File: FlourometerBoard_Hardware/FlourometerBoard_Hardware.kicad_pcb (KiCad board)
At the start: 2 copper layers, 105.4 x 36.8 mm, 14 parts, among them J1 RJ45_LED_Shielded, U1 Teensy4.1_DEV-16771, U3 OKI

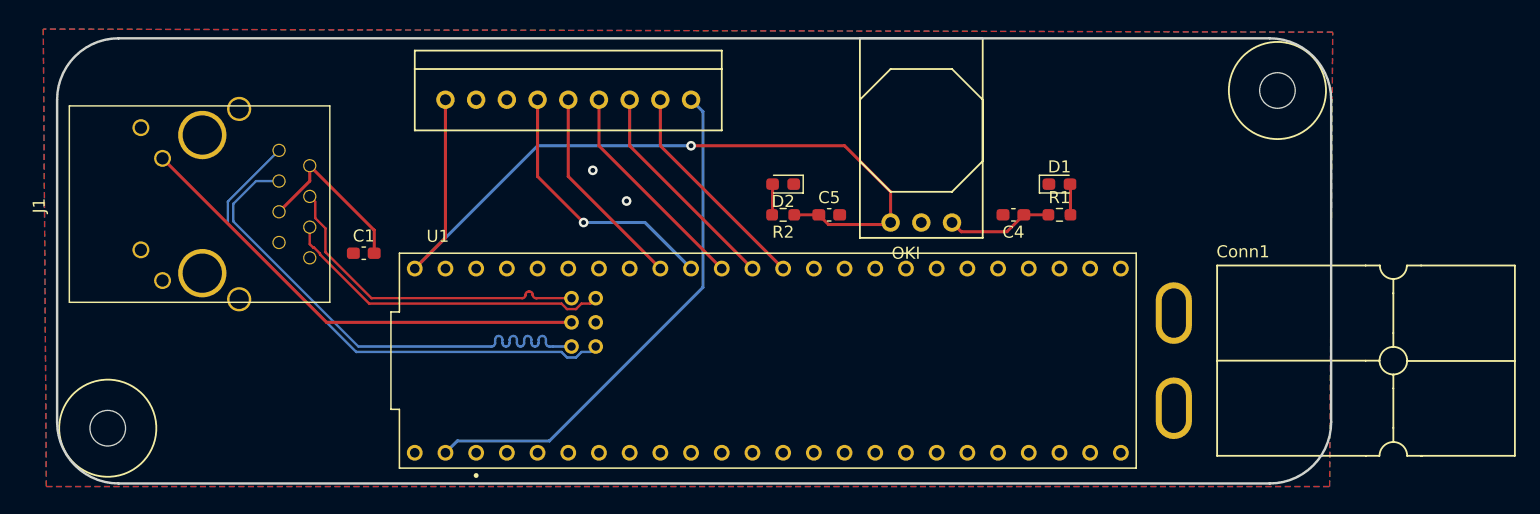
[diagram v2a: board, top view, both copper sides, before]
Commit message: Added LED Breakout Connector to Fluoro Board
Also updated footprint for both boards
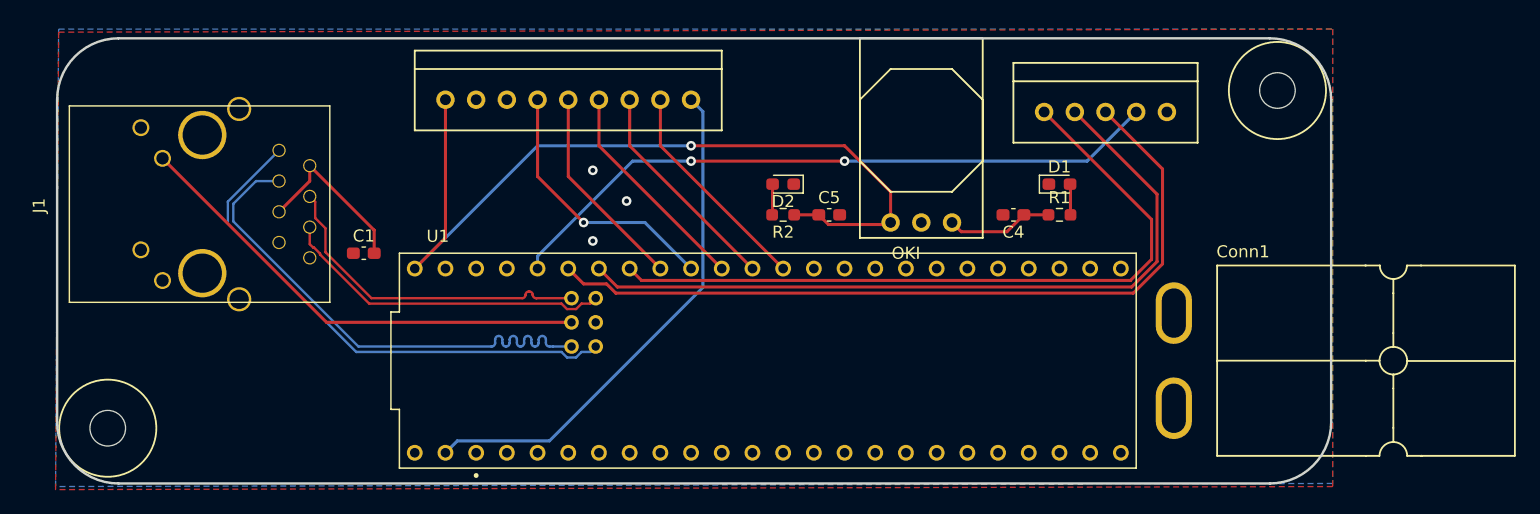
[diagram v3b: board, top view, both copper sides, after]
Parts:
- added Conn3: Molex_SL_05, MRDT_Connectors:MOLEX_SL_05_Vertical, F.Cu at (120.7, 87.4)
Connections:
- net +3V3 renamed +5V
- U1 pad 19: unconnected-(U1-A5-Pad19) -> 530nm LED
- U1 pad 20: unconnected-(U1-A6-Pad20) -> 522nm LED
- U1 pad 21: unconnected-(U1-A7-Pad21) -> 430nm LED
- U1 pad 22: unconnected-(U1-A8-Pad22) -> 400nm LED
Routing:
- net 430nm LED: track 0.00 -> 65.5 mm
- net 522nm LED: track 0.00 -> 62.9 mm
- net 530nm LED: track 0.00 -> 60.2 mm
- net 400nm LED: track 0.00 -> 55.5 mm, vias 0 -> 2
- net GND: vias 2 -> 3
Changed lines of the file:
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@@
   (net 2 "Net-(C1-Pad2)")
   (net 3 "+12V")
-  (net 4 "+3V3")
+  (net 4 "+5V")
   (net 5 "EOS")
   (net 6 "TRG")
@@
   (net 33 "unconnected-(U1-MISO-Pad12)")
   (net 34 "unconnected-(U1-SCK-Pad13)")
-  (net 35 "unconnected-(U1-A5-Pad19)")
-  (net 36 "unconnected-(U1-A6-Pad20)")
-  (net 37 "unconnected-(U1-A7-Pad21)")
-  (net 38 "unconnected-(U1-A8-Pad22)")
+  (net 35 "530nm LED")
+  (net 36 "522nm LED")
+  (net 37 "430nm LED")
+  (net 38 "400nm LED")
   (net 39 "unconnected-(U1-A9-Pad23)")
   (net 40 "unconnected-(U1-A10-Pad24)")
@@
       (stroke (width 0.15) (type solid)) (layer "F.SilkS"))
     (pad "1" thru_hole circle (at 0 0) (size 1.524 1.524) (drill 0.9) (layers "*.Cu" "*.Mask")
-      (net 4 "+3V3") (pintype "input"))
+      (net 4 "+5V") (pintype "input"))
     (pad "2" thru_hole circle (at 2.54 0) (size 1.524 1.524) (drill 0.9) (layers "*.Cu" "*.Mask")
       (net 1 "GND") (pintype "input"))
@@
       (net 1 "GND") (pinfunction "GND") (pintype "output"))
     (pad "3" thru_hole circle (at 5.08 0 180) (size 1.524 1.524) (drill 0.889) (layers "*.Cu" "*.Mask")
-      (net 4 "+3V3") (pinfunction "Vo") (pintype "output"))
+      (net 4 "+5V") (pinfunction "Vo") (pintype "output"))
     (model "${MRDT_KICAD_LIBRARIES}/3D Files/MRDT_Devices/OKI.stp"
       (offset (xyz -2.793999958 1.269999981 3.809999943))
@@
       (net 6 "TRG") (pinfunction "A4") (pintype "bidirectional"))
     (pad "19" thru_hole circle (at -11.43 -7.62) (size 1.308 1.308) (drill 0.8) (layers "*.Cu" "*.Mask")
-      (net 35 "unconnected-(U1-A5-Pad19)") (pinfunction "A5") (pintype "bidirectional+no_connect"))
+      (net 35 "530nm LED") (pinfunction "A5") (pintype "bidirectional"))
     (pad "20" thru_hole circle (at -13.97 -7.62) (size 1.308 1.308) (drill 0.8) (layers "*.Cu" "*.Mask")
-      (net 36 "unconnected-(U1-A6-Pad20)") (pinfunction "A6") (pintype "bidirectional+no_connect"))
+      (net 36 "522nm LED") (pinfunction "A6") (pintype "bidirectional"))
     (pad "21" thru_hole circle (at -16.51 -7.62) (size 1.308 1.308) (drill 0.8) (layers "*.Cu" "*.Mask")
-      (net 37 "unconnected-(U1-A7-Pad21)") (pinfunction "A7") (pintype "bidirectional+no_connect"))
+      (net 37 "430nm LED") (pinfunction "A7") (pintype "bidirectional"))
     (pad "22" thru_hole circle (at -19.05 -7.62) (size 1.308 1.308) (drill 0.8) (layers "*.Cu" "*.Mask")
-      (net 38 "unconnected-(U1-A8-Pad22)") (pinfunction "A8") (pintype "bidirectional+no_connect"))
+      (net 38 "400nm LED") (pinfunction "A8") (pintype "bidirectional"))
     (pad "23" thru_hole circle (at -21.59 -7.62) (size 1.308 1.308) (drill 0.8) (layers "*.Cu" "*.Mask")
       (net 39 "unconnected-(U1-A9-Pad23)") (pinfunction "A9") (pintype "bidirectional+no_connect"))
@@
       (net 17 "T-") (pinfunction "T-") (pintype "bidirectional"))
     (pad "VIN" thru_hole circle (at -29.21 -7.62) (size 1.308 1.308) (drill 0.8) (layers "*.Cu" "*.Mask")
-      (net 4 "+3V3") (pinfunction "VIN") (pintype "input"))
+      (net 4 "+5V") (pinfunction "VIN") (pintype "input"))
     (model "${MRDT_KICAD_LIBRARIES}/3D Files/MRDT_Shields/DEV-16771--3DModel-STEP-418109.STEP"
       (offset (xyz 0 0 0))
@@
       (stroke (width 0.1) (type solid)) (layer "F.Fab"))
     (pad "1" smd roundrect (at -0.8625 0) (size 1.075 0.95) (layers "F.Cu" "F.Paste" "F.Mask") (roundrect_rratio 0.25)
-      (net 4 "+3V3") (pintype "passive"))
+      (net 4 "+5V") (pintype "passive"))
     (pad "2" smd roundrect (at 0.8625 0) (size 1.075 0.95) (layers "F.Cu" "F.Paste" "F.Mask") (roundrect_rratio 0.25)
       (net 1 "GND") (pintype "passive"))
@@
       (stroke (width 0.1) (type solid)) (layer "F.Fab"))
     (pad "1" smd roundrect (at -0.9125 0 180) (size 0.975 0.95) (layers "F.Cu" "F.Paste" "F.Mask") (roundrect_rratio 0.25)
-      (net 4 "+3V3") (pintype "passive"))
+      (net 4 "+5V") (pintype "passive"))
     (pad "2" smd roundrect (at 0.9125 0 180) (size 0.975 0.95) (layers "F.Cu" "F.Paste" "F.Mask") (roundrect_rratio 0.25)
       (net 12 "Net-(D2-A)") (pintype "passive"))
@@
       (scale (xyz 1 1 1))
       (rotate (xyz 0 0 0))
+    )
+  )
+  (footprint "MRDT_Connectors:MOLEX_SL_05_Vertical" (layer "F.Cu")
+    (at 120.65 87.376)
+    (property "Sheetfile" "FlourometerBoard_Hardware.kicad_sch")
+    (property "Sheetname" "")
+    (property "ki_keywords" "MOLEX SL")
+    (attr through_hole)
+    (fp_text reference "Conn3" (at -0.635 3.302) (layer "F.SilkS") hide
+        (effects (font (size 1 1) (thickness 0.15)))
+    )
+    (fp_text value "Molex_SL_05" (at 5.08 3.302) (layer "F.Fab")
+        (effects (font (size 1 1) (thickness 0.15)))
+    )
+    (fp_line (start -2.54 -4.064) (end -2.54 -2.54)
+      (stroke (width 0.15) (type solid)) (layer "F.SilkS"))
+    (fp_line (start -2.54 -2.54) (end 12.7 -2.54)
+      (stroke (width 0.15) (type solid)) (layer "F.SilkS"))
+    (fp_line (start -2.54 2.54) (end -2.54 -2.54)
+      (stroke (width 0.15) (type solid)) (layer "F.SilkS"))
+    (fp_line (start 12.7 -4.064) (end -2.54 -4.064)
+      (stroke (width 0.15) (type solid)) (layer "F.SilkS"))
+    (fp_line (start 12.7 -2.54) (end 12.7 -4.064)
+      (stroke (width 0.15) (type solid)) (layer "F.SilkS"))
+    (fp_line (start 12.7 2.54) (end -2.54 2.54)
+      (stroke (width 0.15) (type solid)) (layer "F.SilkS"))
+    (fp_line (start 12.7 2.54) (end 12.7 -2.54)
+      (stroke (width 0.15) (type solid)) (layer "F.SilkS"))
+    (pad "1" thru_hole circle (at 0 0) (size 1.524 1.524) (drill 0.9) (layers "*.Cu" "*.Mask")
+      (net 35 "530nm LED") (pintype "input"))
+    (pad "2" thru_hole circle (at 2.54 0) (size 1.524 1.524) (drill 0.9) (layers "*.Cu" "*.Mask")
+      (net 36 "522nm LED") (pintype "input"))
+    (pad "3" thru_hole circle (at 5.08 0) (size 1.524 1.524) (drill 0.9) (layers "*.Cu" "*.Mask")
+      (net 37 "430nm LED") (pintype "input"))
+    (pad "4" thru_hole circle (at 7.62 0) (size 1.524 1.524) (drill 0.9) (layers "*.Cu" "*.Mask")
+      (net 38 "400nm LED") (pintype "input"))
+    (pad "5" thru_hole circle (at 10.16 0) (size 1.524 1.524) (drill 0.9) (layers "*.Cu" "*.Mask")
+      (net 1 "GND") (pintype "input"))
+    (model "${MRDT_KICAD_LIBRARIES}/3D Files/MRDT_Connctors/Molex_SL_05_Vertical.stp"
+      (offset (xyz -2.539999962 -2.539999962 13.3349998))
+      (scale (xyz 1 1 1))
+      (rotate (xyz 90 0 0))
     )
   )
@@
   (gr_arc (start 144.399 113.03) (mid 142.911102 116.622102) (end 139.319 118.11)
     (stroke (width 0.2) (type default)) (layer "Edge.Cuts"))
+  (via (at 83.312 98.044) (size 0.8) (drill 0.4) (layers "F.Cu" "B.Cu") (free) (net 1))
   (via (at 83.312 92.202) (size 0.8) (drill 0.4) (layers "F.Cu" "B.Cu") (free) (net 1))
   (via (at 86.106 94.742) (size 0.8) (drill 0.4) (layers "F.Cu" "B.Cu") (free) (net 1))
@@
   (segment (start 82.37845 103.23) (end 83.1 103.23) (width 0.2) (layer "F.Cu") (net 20))
   (segment (start 60.1728 98.591) (end 60.244582 98.591) (width 0.2) (layer "F.Cu") (net 20))
+  (segment (start 129.54 96.266) (end 120.65 87.376) (width 0.254) (layer "F.Cu") (net 35))
+  (segment (start 87.341 101.311) (end 127.797 101.311) (width 0.254) (layer "F.Cu") (net 35))
+  (segment (start 86.36 100.33) (end 87.341 101.311) (width 0.254) (layer "F.Cu") (net 35))
+  (segment (start 127.797 101.311) (end 129.54 99.568) (width 0.254) (layer "F.Cu") (net 35))
+  (segment (start 129.54 99.568) (end 129.54 96.266) (width 0.254) (layer "F.Cu") (net 35))
+  (segment (start 129.994 94.18) (end 123.19 87.376) (width 0.254) (layer "F.Cu") (net 36))
+  (segment (start 85.344 101.854) (end 127.896052 101.854) (width 0.254) (layer "F.Cu") (net 36))
+  (segment (start 127.896052 101.854) (end 129.994 99.756052) (width 0.254) (layer "F.Cu") (net 36))
+  (segment (start 83.82 100.33) (end 85.344 101.854) (width 0.254) (layer "F.Cu") (net 36))
+  (segment (start 129.994 99.756052) (end 129.994 94.18) (width 0.254) (layer "F.Cu") (net 36))
+  (segment (start 130.448 92.094) (end 125.73 87.376) (width 0.254) (layer "F.Cu") (net 37))
+  (segment (start 84.447948 101.6) (end 85.209948 102.362) (width 0.254) (layer "F.Cu") (net 37))
+  (segment (start 81.28 100.33) (end 82.55 101.6) (width 0.254) (layer "F.Cu") (net 37))
+  (segment (start 130.448 99.944104) (end 130.448 92.094) (width 0.254) (layer "F.Cu") (net 37))
+  (segment (start 82.55 101.6) (end 84.447948 101.6) (width 0.254) (layer "F.Cu") (net 37))
+  (segment (start 85.209948 102.362) (end 128.030104 102.362) (width 0.254) (layer "F.Cu") (net 37))
+  (segment (start 128.030104 102.362) (end 130.448 99.944104) (width 0.254) (layer "F.Cu") (net 37))
+  (segment (start 91.44 91.44) (end 104.14 91.44) (width 0.254) (layer "F.Cu") (net 38))
+  (via (at 104.14 91.44) (size 0.8) (drill 0.4) (layers "F.Cu" "B.Cu") (net 38))
+  (via (at 91.44 91.44) (size 0.8) (drill 0.4) (layers "F.Cu" "B.Cu") (net 38))
+  (segment (start 78.74 99.301866) (end 86.601866 91.44) (width 0.254) (layer "B.Cu") (net 38))
+  (segment (start 78.74 100.33) (end 78.74 99.301866) (width 0.254) (layer "B.Cu") (net 38))
+  (segment (start 124.206 91.44) (end 128.27 87.376) (width 0.254) (layer "B.Cu") (net 38))
+  (segment (start 104.14 91.44) (end 124.206 91.44) (width 0.254) (layer "B.Cu") (net 38))
+  (segment (start 86.601866 91.44) (end 91.44 91.44) (width 0.254) (layer "B.Cu") (net 38))
   (zone (net 1) (net_name "GND") (layer "F.Cu") (hatch edge 0.5)
     (connect_pads (clearance 0.5))
@@
     (polygon
       (pts
-        (xy 37.846 80.518)
-        (xy 38.1 118.364)
-        (xy 144.272 118.364)
-        (xy 144.526 80.772)
+        (xy 144.526 80.518)
+        (xy 144.526 118.364)
+        (xy 38.862 118.618)
+        (xy 39.116 80.772)
       )
     )
@@
     (polygon
       (pts
-        (xy 144.272 118.364)
-        (xy 144.526 80.772)
-        (xy 37.846 80.518)
-        (xy 38.1 118.364)
+        (xy 144.526 80.518)
+        (xy 144.526 118.11)
+        (xy 38.862 118.364)
+        (xy 39.116 80.518)
       )
     )

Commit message: Added 5V to LED connectors
Also added FETs to LEDs on breakout.
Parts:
- Conn3: value Molex_SL_05 -> Molex_SL_07; footprint MRDT_Connectors:MOLEX_SL_05_Vertical -> MRDT_Connectors:MOLEX_SL_07_Vertical
- moved Conn3 2.74 mm to (118.1, 88.4)
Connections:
- Conn3 pad 5: GND -> +5V
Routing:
- net +5V: track 71.1 -> 96.5 mm
- net 400nm LED: track 55.5 -> 52.5 mm
- net 530nm LED: track 60.2 -> 62.3 mm
- net 430nm LED: track 65.5 -> 67.7 mm
- net 522nm LED: track 62.9 -> 65.0 mm

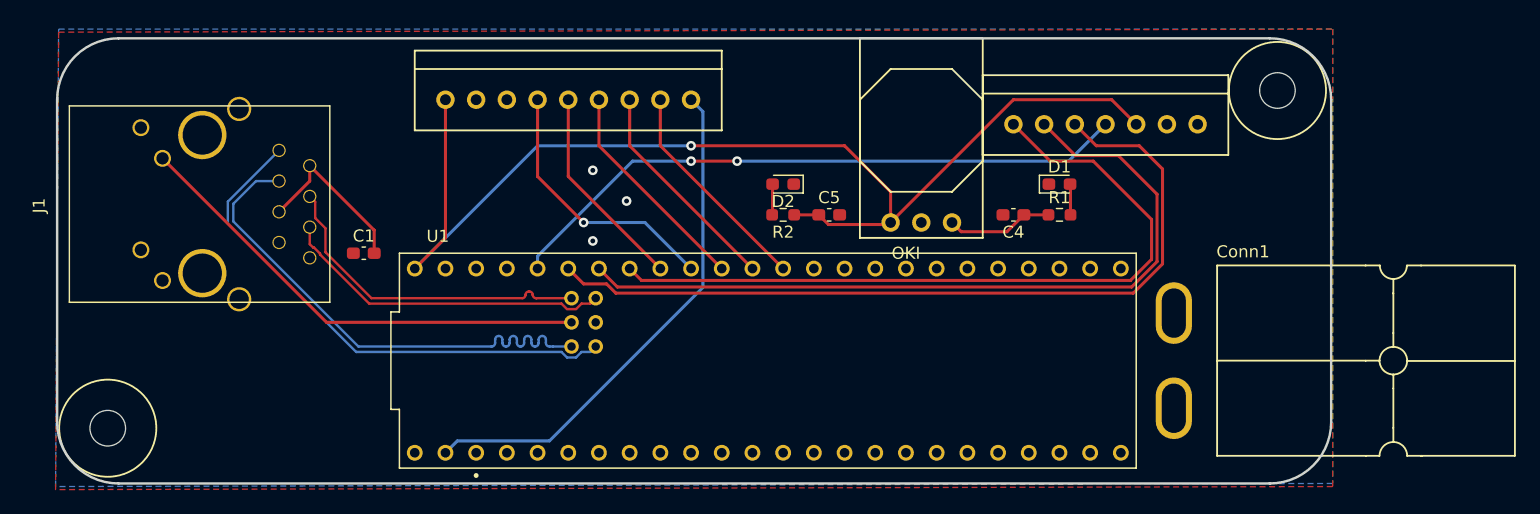
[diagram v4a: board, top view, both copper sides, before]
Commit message: Changes made based on layout review notes
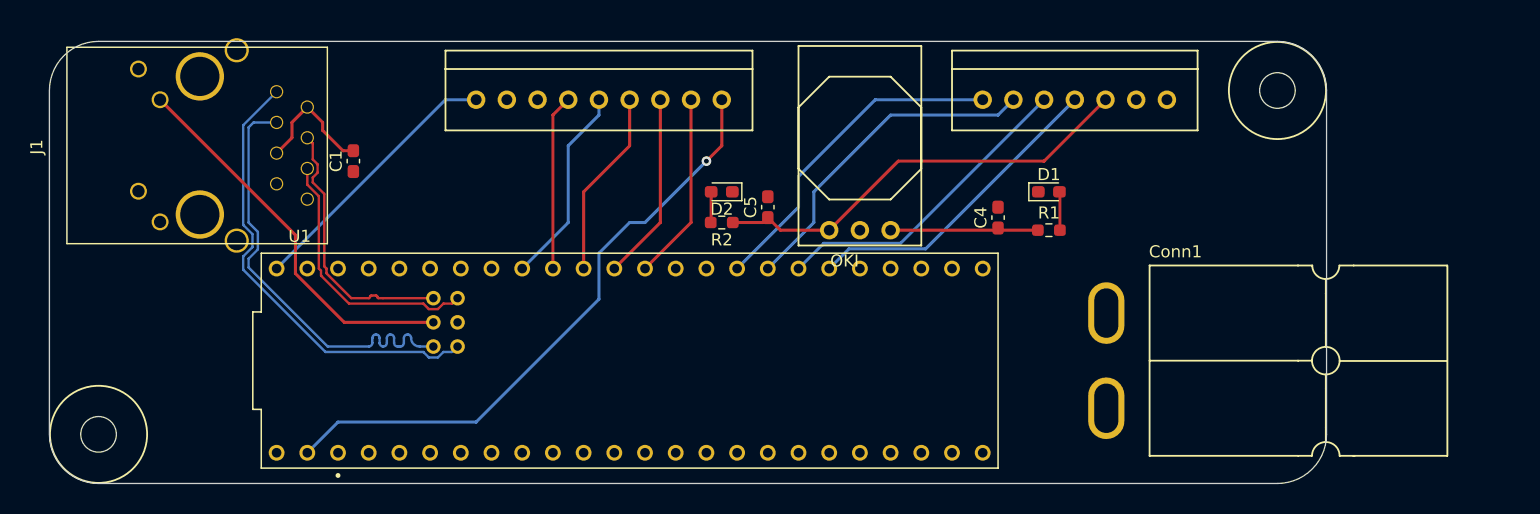
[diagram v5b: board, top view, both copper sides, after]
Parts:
- moved U1 11.4 mm to (86.4, 108.0)
- moved C1 7.67 mm to (63.5, 91.4), turned to 90 degrees
- moved Conn1 5.59 mm to (125.7, 112.2)
- moved C5 5.12 mm to (97.8, 95.2), turned to 90 degrees
- moved D2 5.12 mm to (94.0, 94.0)
- moved U3 5.12 mm to (108.0, 97.2)
- moved R2 5.12 mm to (94.0, 96.5)
- moved J1 4.86 mm to (37.8, 90.3)
- moved Conn3 3.25 mm to (115.6, 86.4)
- moved Conn2 2.54 mm to (73.7, 86.4)
- moved R1 1.54 mm to (121.0, 97.2)
- moved C4 1.29 mm to (116.8, 96.1), turned to 90 degrees
- moved D1 1.08 mm to (121.0, 94.0)
- moved REF** 0.92 mm to (42.4, 114.0)
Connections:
- U1 pad 19: 530nm LED -> unconnected-(U1-A5-Pad19)
- U1 pad 20: 522nm LED -> unconnected-(U1-A6-Pad20)
- U1 pad 21: 430nm LED -> unconnected-(U1-A7-Pad21)
- U1 pad 22: 400nm LED -> unconnected-(U1-A8-Pad22)
- U1 pad 38: unconnected-(U1-A14-Pad38) -> 400nm LED
- U1 pad 39: unconnected-(U1-A15-Pad39) -> 430nm LED
- U1 pad 40: unconnected-(U1-A16-Pad40) -> 522nm LED
- U1 pad 41: unconnected-(U1-A17-Pad41) -> 530nm LED
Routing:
- net 430nm LED: track 67.7 -> 26.1 mm
- net +5V: track 96.5 -> 58.2 mm, vias 1 -> 0
- net 522nm LED: track 65.0 -> 27.6 mm
- net 530nm LED: track 62.3 -> 27.6 mm
- net 400nm LED: track 52.5 -> 26.1 mm, vias 2 -> 0
- net WHITE_LED: track 42.9 -> 50.9 mm, vias 0 -> 1
- net EOS: track 22.2 -> 14.5 mm, vias 1 -> 0
- net LED: track 39.5 -> 32.1 mm
- net T-: track 43.0 -> 36.8 mm
- net T+: track 43.2 -> 37.6 mm
- net R-: track 27.7 -> 22.1 mm
- net R+: track 27.7 -> 22.1 mm
- net Net-(C1-Pad2): track 14.3 -> 10.6 mm
- net +12V: track 8.87 -> 12.3 mm
- net START: track 18.2 -> 15.5 mm
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- removed copper zone on B.Cu, net GND
- removed copper zone on F.Cu, net GND
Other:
- board size 105.4 x 36.8 mm -> 105.7 x 36.6 mm
